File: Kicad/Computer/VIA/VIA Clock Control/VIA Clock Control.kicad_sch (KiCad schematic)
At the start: 27 parts, among them IC10 74LVC1G157GV-Q100H, IC2 74LVC4245APW,118, IC2 AP7365-33WG-7, IC5 74LVC244APW,118, IC7 74LVC74APW,118, IC8 74LVC257APW,118, IC9 74LVC257APW,118, J1 Conn_02x16_Counter_Clockwise

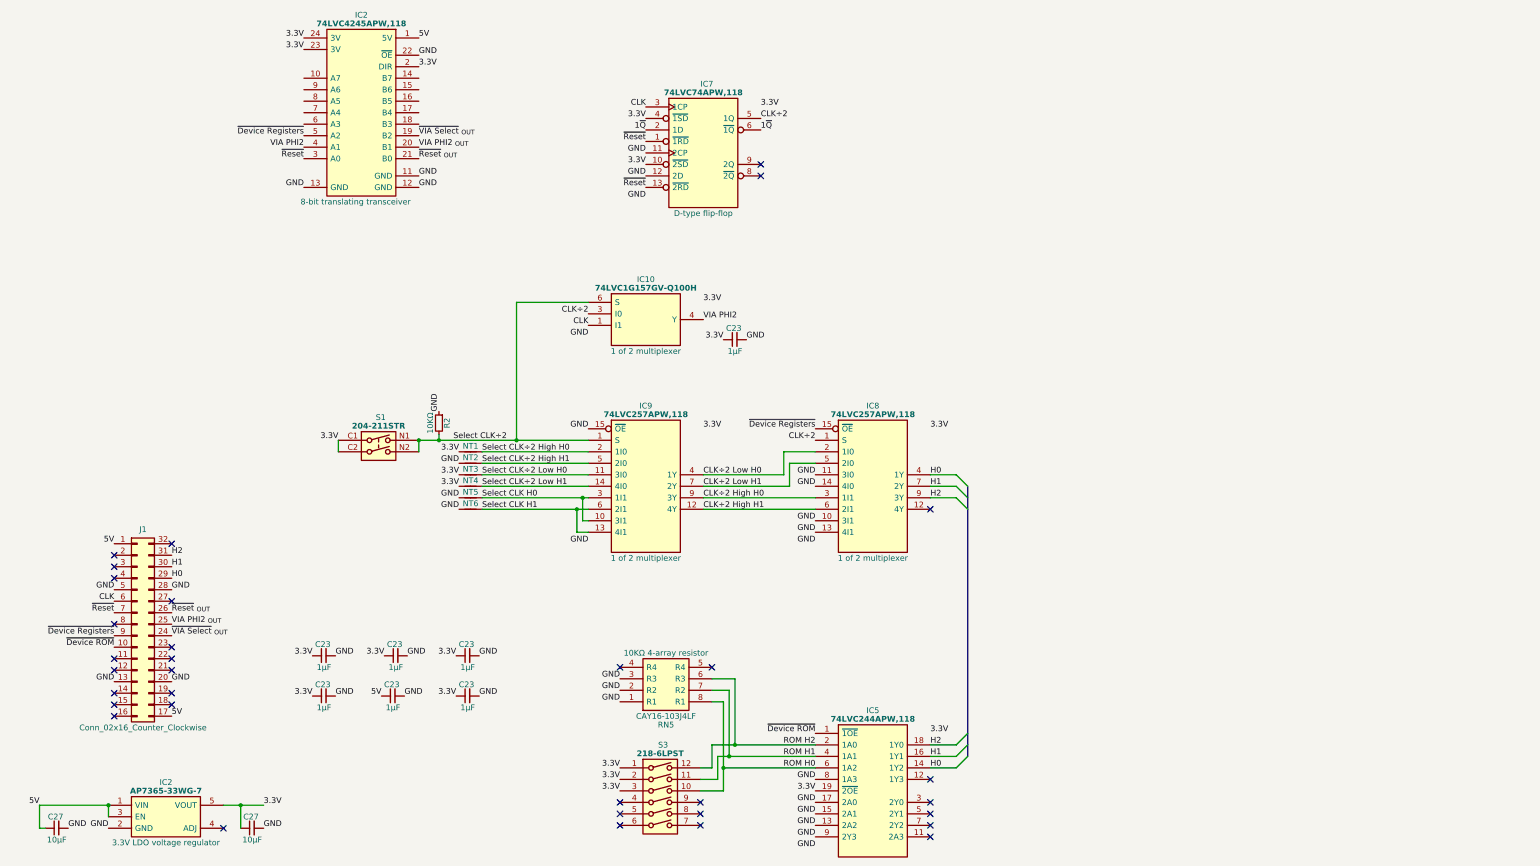
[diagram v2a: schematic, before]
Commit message: Standardising DIP board layouts.
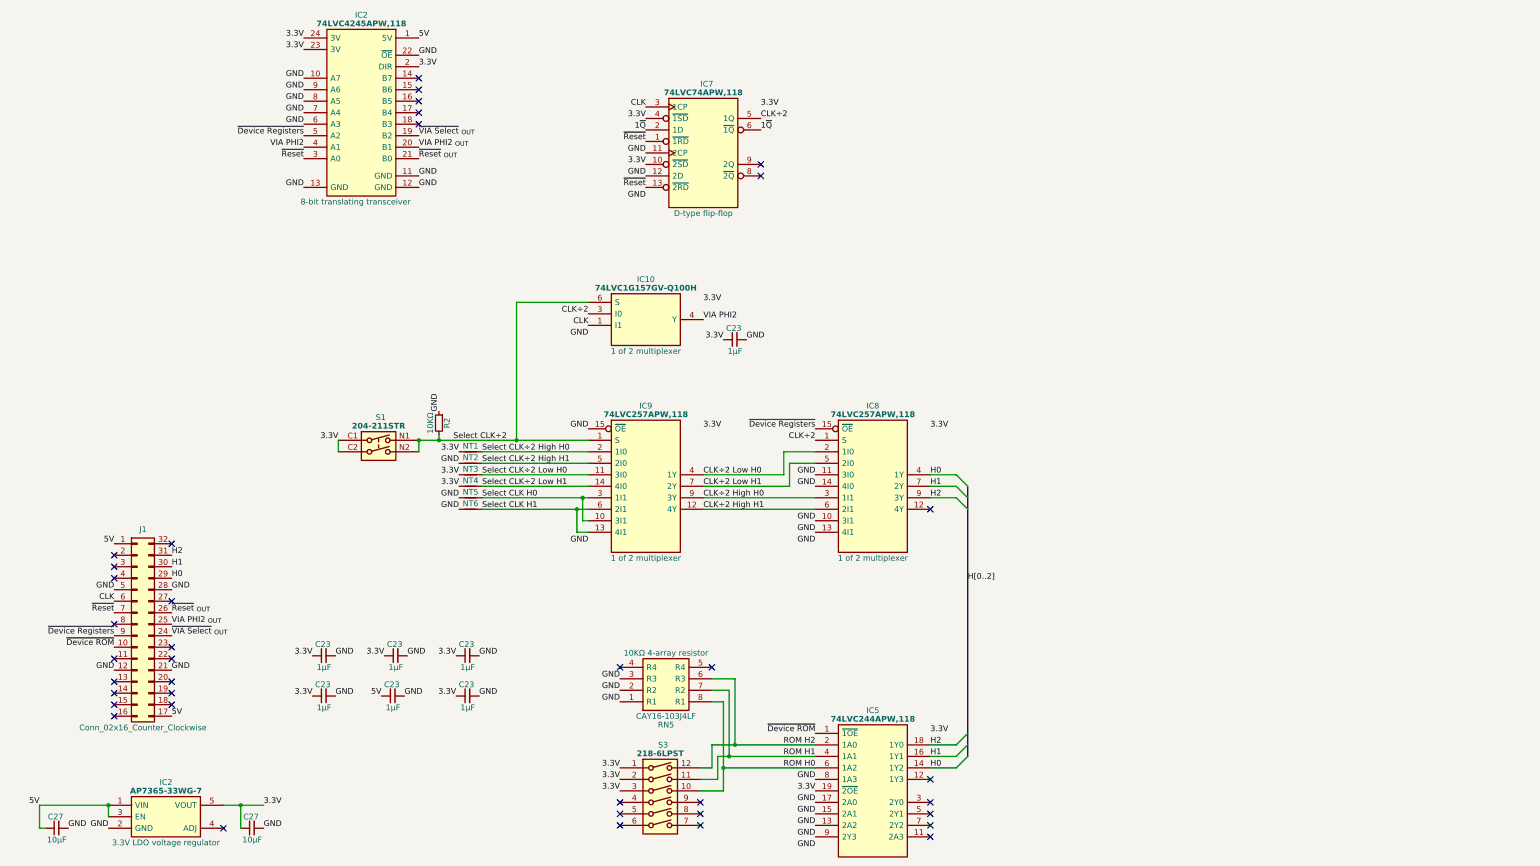
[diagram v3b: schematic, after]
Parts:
- IC2: Silkscreen 74LVC4245APW -> 74LVC4245
- S1: Arrow Part Number 204-211STR -> (none); Arrow Price/Stock https://www.arrow.com/en/products/204-211str/cts -> (none)
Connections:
- net GND: now also IC2.10 (A7), IC2.6 (A3), IC2.7 (A4), IC2.8 (A5), IC2.9 (A6), J1.12 (Pin_12), J1.21 (Pin_21); no longer J1.13 (Pin_13), J1.20 (Pin_20)
- no-connect marks 33 -> 38
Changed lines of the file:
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@@
   )
   (no_connect (at -48.26 149.86))
-  (no_connect (at -48.26 175.26))
+  (no_connect (at -48.26 177.8))
   (no_connect (at 63.5 207.01))
   (no_connect (at -48.26 182.88))
@@
   (no_connect (at -35.56 180.34))
   (no_connect (at -35.56 182.88))
+  (no_connect (at 19.05 54.61))
   (no_connect (at 132.08 209.55))
+  (no_connect (at 19.05 46.99))
   (no_connect (at 63.5 174.625))
   (no_connect (at -35.56 160.02))
@@
   (no_connect (at 132.08 139.7))
   (no_connect (at 94.615 63.5))
+  (no_connect (at 19.05 49.53))
   (no_connect (at -48.26 165.1))
   (no_connect (at -48.26 172.72))
@@
   (no_connect (at -24.13 210.185))
   (no_connect (at -48.26 154.94))
+  (no_connect (at 19.05 52.07))
+  (no_connect (at 19.05 44.45))
   (no_connect (at 132.08 207.01))
   (no_connect (at -48.26 152.4))
-  (no_connect (at -35.56 175.26))
+  (no_connect (at -35.56 177.8))
   (no_connect (at 83.82 174.625))
   (no_connect (at -35.56 170.18))
@@
     (effects (font (size 1.27 1.27)) (justify left bottom))
   )
+  (label "GND" (at -6.35 49.53 180) (fields_autoplaced)
+    (effects (font (size 1.27 1.27)) (justify right bottom))
+  )
   (label "GND" (at 32.385 172.085 0) (fields_autoplaced)
     (effects (font (size 1.27 1.27)) (justify left bottom))
@@
     (effects (font (size 1.27 1.27)) (justify right bottom))
   )
-  (label "GND" (at -48.26 177.8 180) (fields_autoplaced)
+  (label "GND" (at -48.26 175.26 180) (fields_autoplaced)
     (effects (font (size 1.27 1.27)) (justify right bottom))
   )
@@
     (effects (font (size 1.27 1.27)) (justify right bottom))
   )
+  (label "GND" (at -6.35 44.45 180) (fields_autoplaced)
+    (effects (font (size 1.27 1.27)) (justify right bottom))
+  )
   (label "5V" (at -64.77 205.105 180) (fields_autoplaced)
     (effects (font (size 1.27 1.27)) (justify right bottom))
@@
     (effects (font (size 1.27 1.27)) (justify left bottom))
   )
+  (label "GND" (at -6.35 52.07 180) (fields_autoplaced)
+    (effects (font (size 1.27 1.27)) (justify right bottom))
+  )
   (label "GND" (at 63.5 177.165 180) (fields_autoplaced)
     (effects (font (size 1.27 1.27)) (justify right bottom))
@@
     (effects (font (size 1.27 1.27)) (justify right bottom))
   )
-  (label "GND" (at -35.56 177.8 0) (fields_autoplaced)
+  (label "GND" (at -35.56 175.26 0) (fields_autoplaced)
     (effects (font (size 1.27 1.27)) (justify left bottom))
   )
@@
     (effects (font (size 1.27 1.27)) (justify left bottom))
   )
+  (label "GND" (at -6.35 54.61 180) (fields_autoplaced)
+    (effects (font (size 1.27 1.27)) (justify right bottom))
+  )
+  (label "GND" (at -6.35 46.99 180) (fields_autoplaced)
+    (effects (font (size 1.27 1.27)) (justify right bottom))
+  )
   (label "GND" (at -6.35 68.58 180) (fields_autoplaced)
     (effects (font (size 1.27 1.27)) (justify right bottom))
@@
   )
   (label "3.3V" (at 81.915 93.98 0) (fields_autoplaced)
+    (effects (font (size 1.27 1.27)) (justify left bottom))
+  )
+  (label "H[0..2]" (at 140.335 155.575 0) (fields_autoplaced)
     (effects (font (size 1.27 1.27)) (justify left bottom))
   )
@@
     )
   )
-  (symbol (lib_name "C_0805_5") (lib_id "HCP65:C_0805") (at -63.5 210.185 0) (unit 1)
+  (symbol (lib_id "HCP65:C_0805") (at -63.5 210.185 0) (unit 1)
     (in_bom yes) (on_board yes) (dnp no)
     (property "Reference" "C27" (at -61.214 207.645 0)
@@
     )
   )
-  (symbol (lib_name "C_0805_5") (lib_id "HCP65:C_0805") (at -20.32 210.185 0) (unit 1)
+  (symbol (lib_id "HCP65:C_0805") (at -20.32 210.185 0) (unit 1)
     (in_bom yes) (on_board yes) (dnp no)
     (property "Reference" "C27" (at -18.034 207.645 0)
@@
       (effects (font (size 1.27 1.27)) (justify left) hide)
     )
-    (property "Silkscreen" "74LVC4245APW" (at 6.604 74.168 0)
+    (property "Silkscreen" "74LVC4245" (at 6.604 74.168 0)
       (effects (font (size 1.27 1.27)) hide)
     )
@@
       (effects (font (size 1.27 1.27)) (justify left) hide)
     )
-    (property "Arrow Part Number" "204-211STR" (at 21.59 161.29 0)
-      (effects (font (size 1.27 1.27)) (justify left) hide)
-    )
-    (property "Arrow Price/Stock" "https://www.arrow.com/en/products/204-211str/cts" (at 21.59 163.83 0)
-      (effects (font (size 1.27 1.27)) (justify left) hide)
-    )

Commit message: Updated forgotten VIA Clock Control.
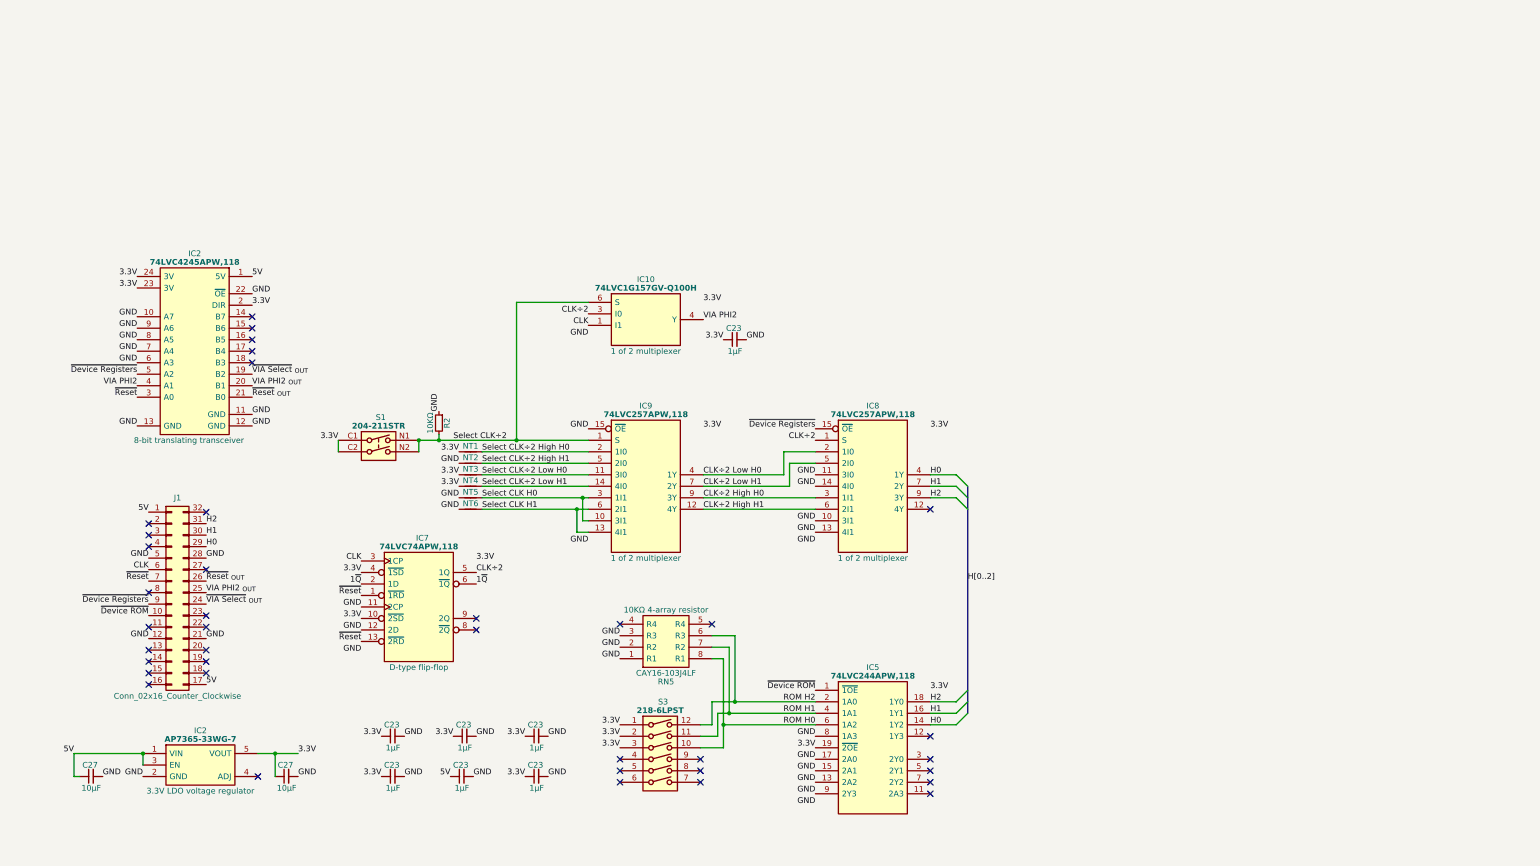
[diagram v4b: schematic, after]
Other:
- moved on the sheet: C23, C27, IC2, IC5, IC7, J1, RN5, S3

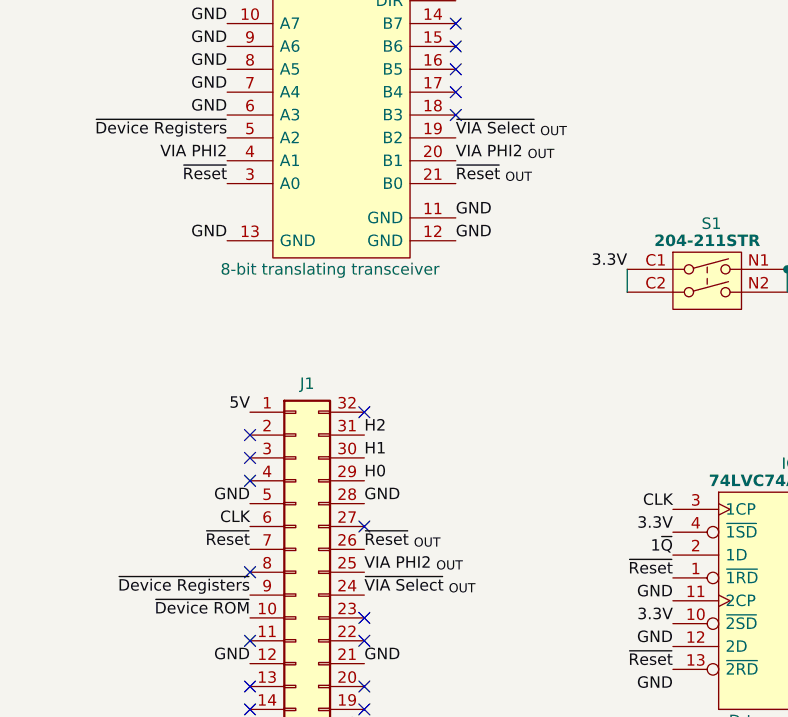
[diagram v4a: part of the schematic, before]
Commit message: Re-routed all Boards.
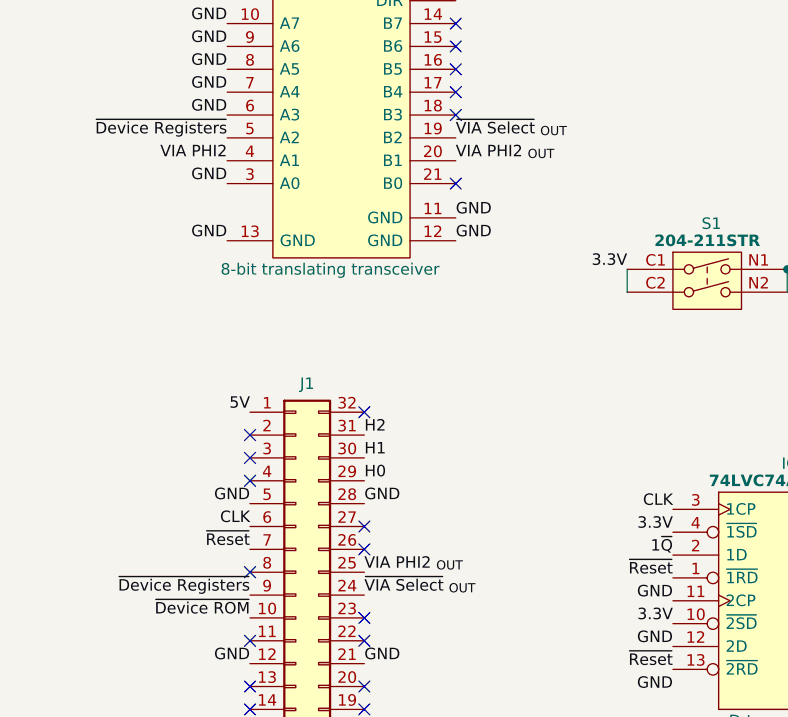
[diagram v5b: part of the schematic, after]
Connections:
- net GND: now also IC2.3 (A0)
- net ~{Reset}: no longer IC2.3 (A0)
- net ~{Reset} _{OUT}: no longer names the net of IC2.21 (B0)
- net ~{Reset} _{OUT}: no longer J1.26 (Pin_26)
- no-connect marks 38 -> 40
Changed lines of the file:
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@@
   (no_connect (at 63.5 200.025))
   (no_connect (at -27.94 173.355))
+  (no_connect (at -27.94 155.575))
   (no_connect (at -27.94 175.895))
   (no_connect (at -17.78 107.315))
@@
   (no_connect (at -40.64 147.955))
   (no_connect (at -17.78 104.775))
+  (no_connect (at -17.78 114.935))
   (no_connect (at -17.78 97.155))
   (no_connect (at 132.08 197.485))
@@
     (effects (font (size 1.27 1.27)) (justify left bottom))
   )
-  (label "~{Reset} _{OUT}" (at -27.94 155.575 0) (fields_autoplaced)
-    (effects (font (size 1.27 1.27)) (justify left bottom))
-  )
   (label "3.3V" (at 10.795 189.865 180) (fields_autoplaced)
     (effects (font (size 1.27 1.27)) (justify right bottom))
@@
     (effects (font (size 1.27 1.27)) (justify right bottom))
   )
+  (label "GND" (at -43.18 114.935 180) (fields_autoplaced)
+    (effects (font (size 1.27 1.27)) (justify right bottom))
+  )
   (label "5V" (at -40.64 140.335 180) (fields_autoplaced)
     (effects (font (size 1.27 1.27)) (justify right bottom))
@@
     (effects (font (size 1.27 1.27)) (justify left bottom))
   )
-  (label "~{Reset} _{OUT}" (at -17.78 114.935 0) (fields_autoplaced)
-    (effects (font (size 1.27 1.27)) (justify left bottom))
-  )
   (label "~{VIA Select} _{OUT}" (at -17.78 109.855 0) (fields_autoplaced)
     (effects (font (size 1.27 1.27)) (justify left bottom))
@@
     (effects (font (size 1.27 1.27)) (justify left bottom))
   )
-  (label "~{Reset}" (at -43.18 114.935 180) (fields_autoplaced)
-    (effects (font (size 1.27 1.27)) (justify right bottom))
-  )
   (label "~{Device Registers}" (at 106.68 121.92 180) (fields_autoplaced)
